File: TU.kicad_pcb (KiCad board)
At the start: 4 copper layers, 48.3 x 109.2 mm, 134 parts, among them IC1 CC1190, J1 Conn_01x06_Male, J2 Conn_01x17_Male, J3 Conn_01x05_Male, J4 Debugger connector, J5 ARM_JTAG_SWD_10, J6 Conn_01x05_Male, U1 ADP150AUJZ-3.3-R7, U2 SN65HVD233, U3 CC1200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

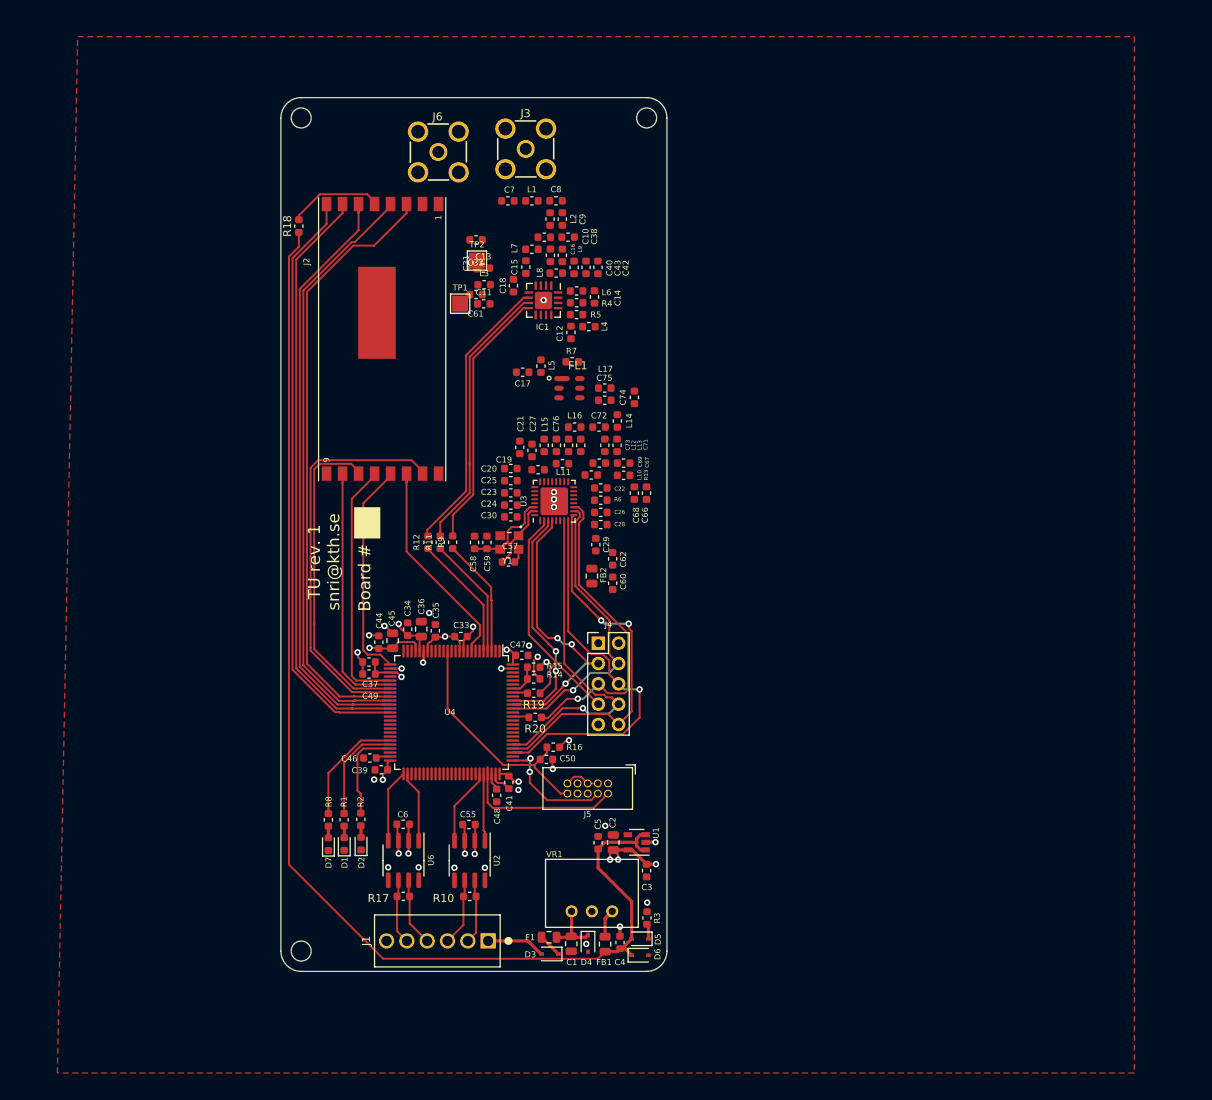
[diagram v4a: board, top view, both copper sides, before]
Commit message: Routed power for RF
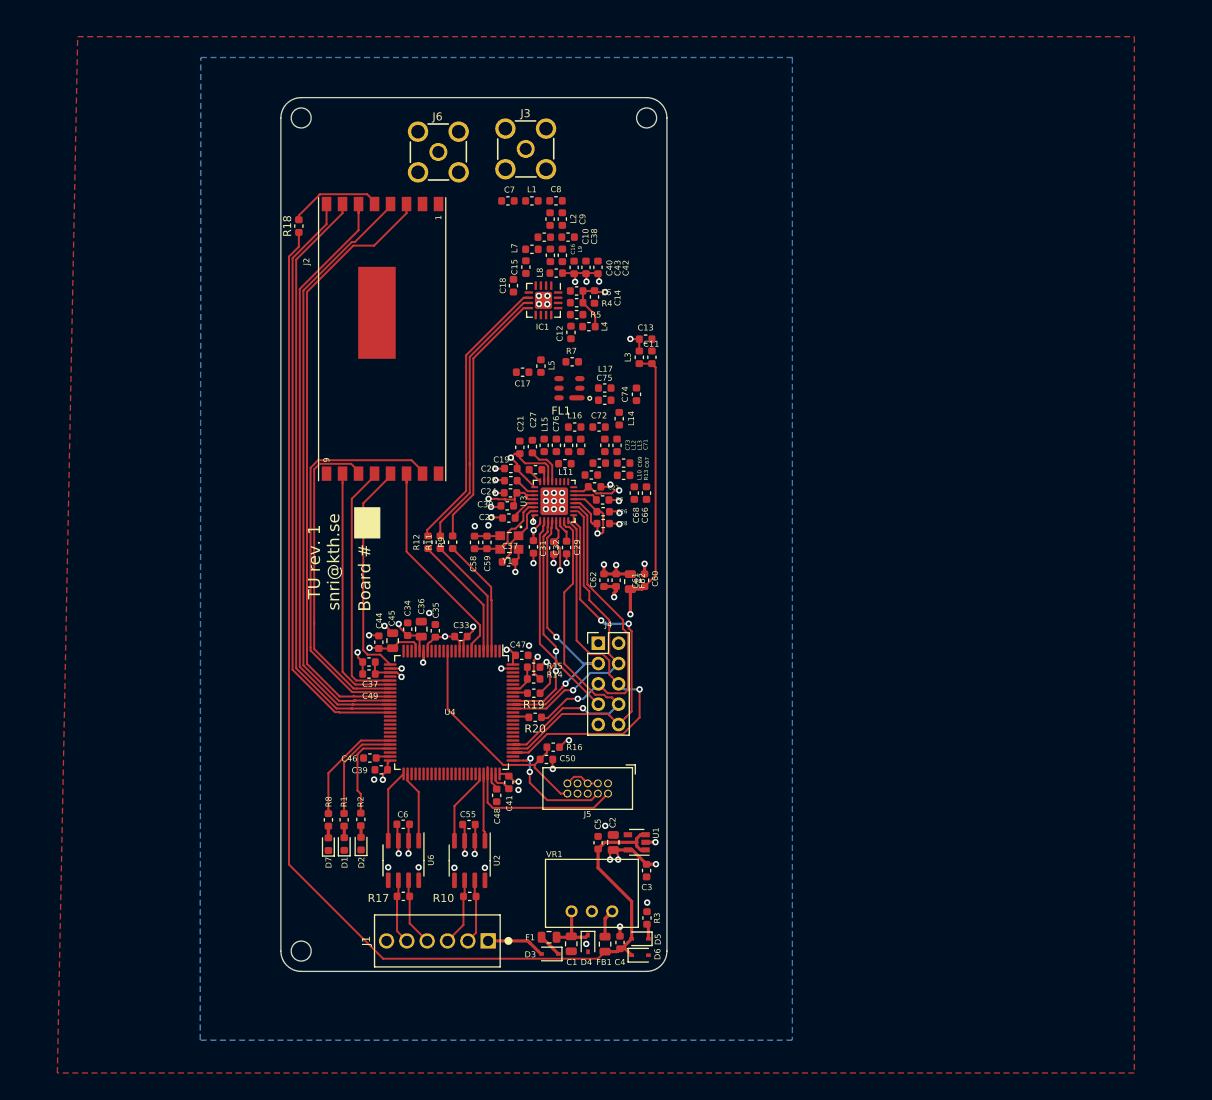
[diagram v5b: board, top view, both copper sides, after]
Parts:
- removed TP1: VDD_CC1190, TestPoint:TestPoint_Pad_2.0x2.0mm
- removed TP2: VDD_CC1200, TestPoint:TestPoint_Pad_2.0x2.0mm
- moved C61 39.8 mm to (113.0, 90.8), turned to 270 degrees
- moved C32 39.0 mm to (102.7, 86.6), turned to 270 degrees
- moved C31 36.9 mm to (105.2, 86.8)
- moved C13 22.1 mm to (116.7, 60.7)
- moved C11 22.1 mm to (117.5, 62.9), turned to 90 degrees
- moved L3 21.4 mm to (115.9, 62.9), turned to 90 degrees
- moved FB2 4.87 mm to (114.8, 91.0)
- moved C60 4.01 mm to (116.6, 90.8)
- moved C29 3.67 mm to (106.8, 86.7)
- moved C23 3.15 mm to (99.6, 83.0)
- moved C62 2.89 mm to (111.5, 90.8), turned to 270 degrees
- moved C24 1.53 mm to (99.8, 79.9)
- moved C30 1.45 mm to (99.4, 81.5)
- moved C22 0.79 mm to (110.3, 79.1)
- moved C27 0.48 mm to (102.6, 74.1)
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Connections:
- net Net-(C13-Pad1) renamed /CC1190/VDD_CC1190
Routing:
- net /transceiver/VDD_CC1200: track 0.00 -> 57.1 mm, vias 0 -> 8
- net +3V3: track 55.1 -> 90.1 mm, vias 14 -> 15
- net GND: track 36.9 -> 61.7 mm, vias 28 -> 55
- net /CC1190/VDD_CC1190: track 0.00 -> 18.3 mm, vias 0 -> 5
- net Net-(C27-Pad1): track 0.00 -> 5.19 mm
- net Net-(C23-Pad1): track 0.00 -> 4.14 mm
- net Net-(R6-Pad2): track 0.00 -> 3.06 mm
- net Net-(C29-Pad1): track 0.00 -> 2.95 mm
- net Net-(C25-Pad1): track 0.00 -> 2.74 mm
- net Net-(C19-Pad2): track 0.00 -> 1.96 mm
- net Net-(C19-Pad1): track 0.00 -> 1.51 mm
- net /transceiver/GPIO3: track 29.4 -> 28.2 mm
- net /MOSI: track 43.5 -> 44.6 mm
- net /~RESET: track 32.0 -> 30.9 mm
- net /GPIO0: track 37.6 -> 36.7 mm
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- added copper zone on In2.Cu, net /CC1190/VDD_CC1190
- added copper zone on In2.Cu, net /transceiver/VDD_CC1200
- added copper zone on B.Cu, net GND

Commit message: Feedback from peer review
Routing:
- net Net-(J2-Pad5): track 12.1 -> 13.0 mm

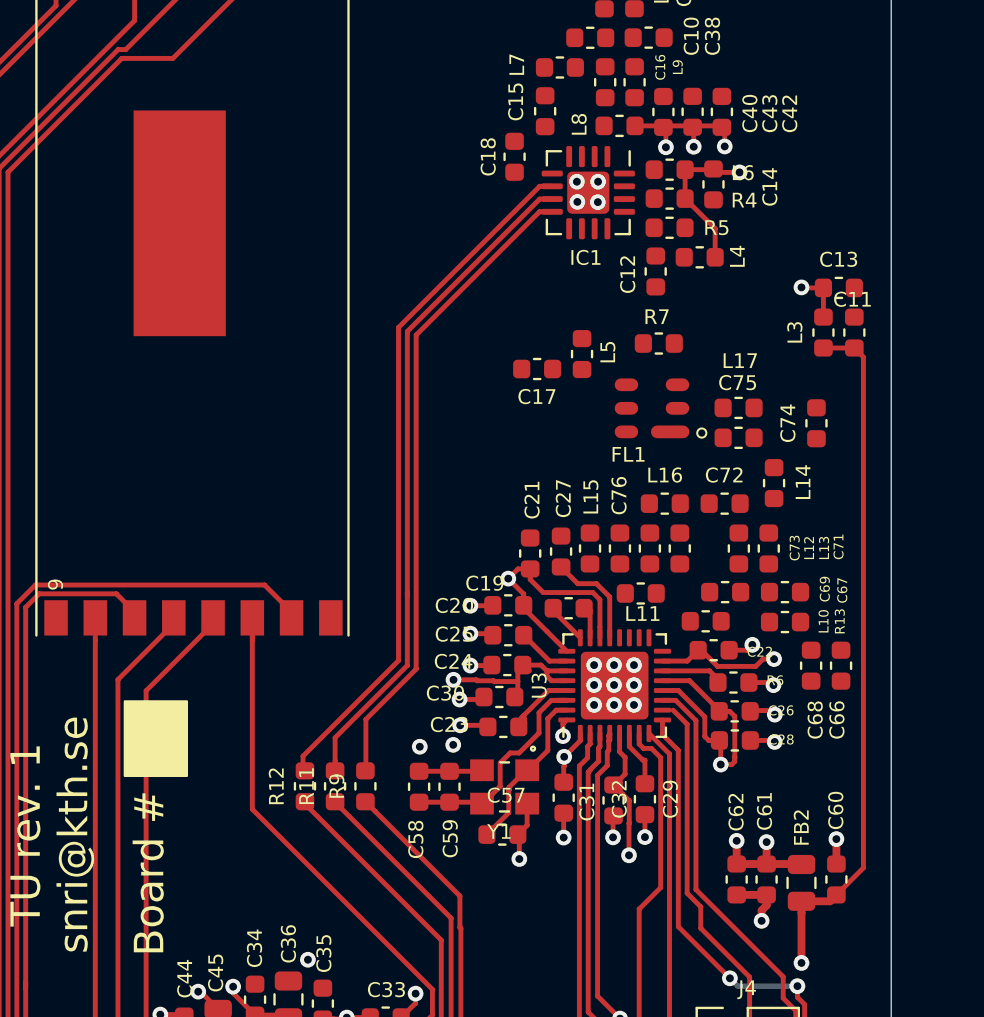
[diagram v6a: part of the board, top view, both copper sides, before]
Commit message: Added heatpad vias for extra rf module.
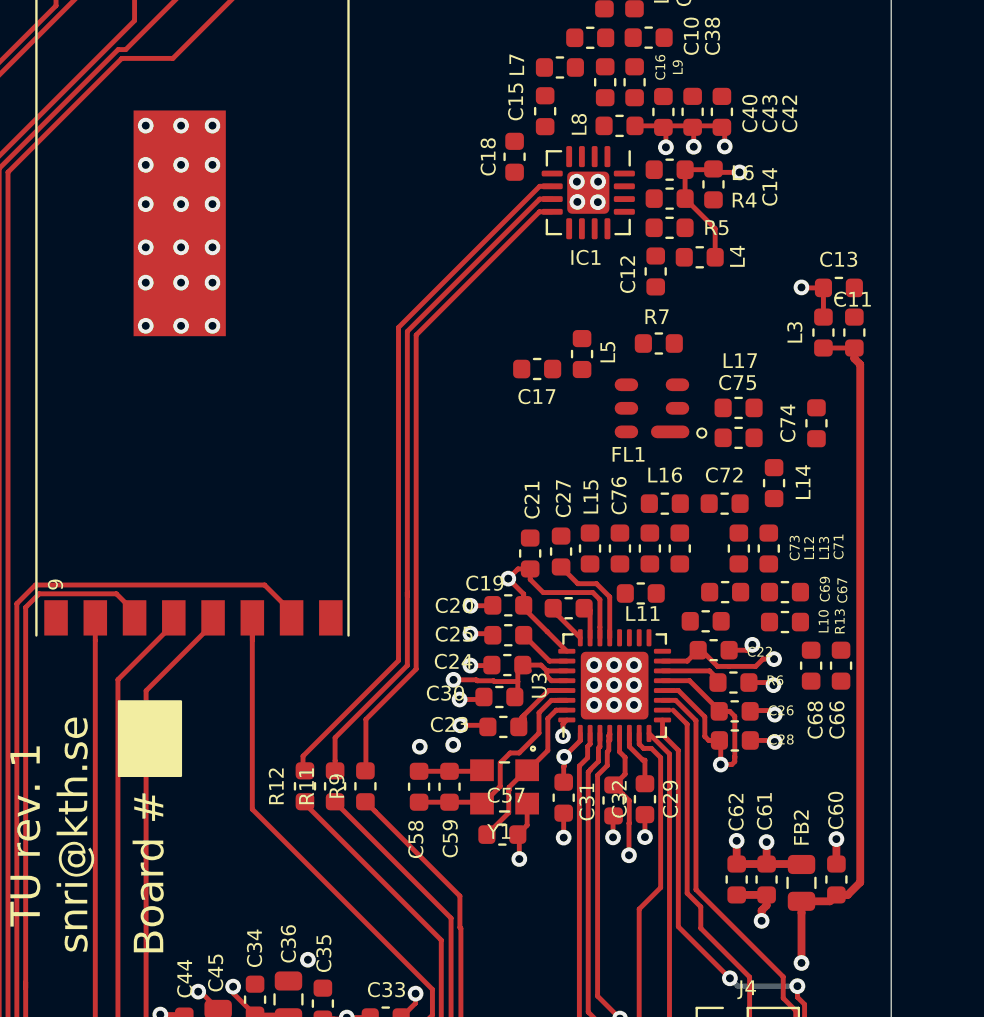
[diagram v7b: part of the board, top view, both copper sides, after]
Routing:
- net GND: vias 55 -> 73
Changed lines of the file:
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@@
     (thickness 1.6)
     (drawings 28)
-    (tracks 799)
+    (tracks 819)
     (zones 0)
     (modules 132)
@@
   )
   (setup
-    (last_trace_width 0.25)
+    (last_trace_width 0.4)
     (user_trace_width 0.4)
     (trace_clearance 0.2)
@@
     (effects (font (size 1.5 1.5) (thickness 0.3)))
   )
-  (gr_poly (pts (xy 80.3275 85.5345) (xy 83.5025 85.5345) (xy 83.5025 81.7245) (xy 80.3275 81.7245)) (layer F.SilkS) (width 0.1))
+  (gr_poly (pts (xy 80.025 85.5345) (xy 83.2 85.5345) (xy 83.2 81.7245) (xy 80.025 81.7245)) (layer F.SilkS) (width 0.1))
   (gr_text "TU rev. 1\nsnri@kth.se\n" (at 76.5175 88.519 90) (layer F.SilkS)
     (effects (font (size 1.5 1.5) (thickness 0.3)))
   )
+  (via (at 81.4 62.6) (size 0.8) (drill 0.4) (layers F.Cu B.Cu) (net 1))
+  (via (at 84.8 62.6) (size 0.8) (drill 0.4) (layers F.Cu B.Cu) (net 1))
+  (via (at 83.2 62.6) (size 0.8) (drill 0.4) (layers F.Cu B.Cu) (net 1))
+  (via (at 81.4 60.4) (size 0.8) (drill 0.4) (layers F.Cu B.Cu) (net 1))
+  (via (at 84.8 60.4) (size 0.8) (drill 0.4) (layers F.Cu B.Cu) (net 1))
+  (via (at 83.2 60.4) (size 0.8) (drill 0.4) (layers F.Cu B.Cu) (net 1))
+  (via (at 81.4 58.6) (size 0.8) (drill 0.4) (layers F.Cu B.Cu) (net 1))
+  (via (at 84.8 58.6) (size 0.8) (drill 0.4) (layers F.Cu B.Cu) (net 1))
+  (via (at 83.2 58.6) (size 0.8) (drill 0.4) (layers F.Cu B.Cu) (net 1))
+  (via (at 81.4 56.4) (size 0.8) (drill 0.4) (layers F.Cu B.Cu) (net 1))
+  (via (at 84.8 56.4) (size 0.8) (drill 0.4) (layers F.Cu B.Cu) (net 1))
+  (via (at 83.2 56.4) (size 0.8) (drill 0.4) (layers F.Cu B.Cu) (net 1))
+  (via (at 81.4 54.4) (size 0.8) (drill 0.4) (layers F.Cu B.Cu) (net 1))
+  (via (at 84.8 54.4) (size 0.8) (drill 0.4) (layers F.Cu B.Cu) (net 1))
+  (via (at 83.2 54.4) (size 0.8) (drill 0.4) (layers F.Cu B.Cu) (net 1))
+  (via (at 84.8 52.4) (size 0.8) (drill 0.4) (layers F.Cu B.Cu) (net 1))
+  (via (at 83.2 52.4) (size 0.8) (drill 0.4) (layers F.Cu B.Cu) (net 1))
+  (via (at 81.4 52.4) (size 0.8) (drill 0.4) (layers F.Cu B.Cu) (net 1))
   (via (at 104.4321 56.2991) (size 0.8) (drill 0.4) (layers F.Cu B.Cu) (net 1))
   (via (at 103.3907 56.2864) (size 0.8) (drill 0.4) (layers F.Cu B.Cu) (net 1))
@@
   (segment (start 114.808 94.742) (end 114.808 94.742) (width 0.4) (layer F.Cu) (net 3))
   (via (at 114.808 95.0595) (size 0.8) (drill 0.4) (layers F.Cu B.Cu) (net 3))
-  (segment (start 117.962012 64.190312) (end 117.5004 63.7287) (width 0.25) (layer F.Cu) (net 3))
-  (segment (start 117.962012 90.216488) (end 117.962012 64.190312) (width 0.25) (layer F.Cu) (net 3))
-  (segment (start 116.586 91.5925) (end 117.962012 90.216488) (width 0.25) (layer F.Cu) (net 3))
+  (segment (start 117.161 91.5925) (end 117.8 90.9535) (width 0.4) (layer F.Cu) (net 3))
+  (segment (start 116.586 91.5925) (end 117.161 91.5925) (width 0.4) (layer F.Cu) (net 3))
+  (segment (start 117.5004 64.2662) (end 117.5004 63.7287) (width 0.4) (layer F.Cu) (net 3))
+  (segment (start 117.8 64.5658) (end 117.5004 64.2662) (width 0.4) (layer F.Cu) (net 3))
+  (segment (start 117.8 90.9535) (end 117.8 64.5658) (width 0.4) (layer F.Cu) (net 3))
   (segment (start 116.076838 122.61614) (end 116.70184 122.61614) (width 0.4) (layer F.Cu) (net 4))
   (segment (start 115.5993 123.093678) (end 116.076838 122.61614) (width 0.4) (layer F.Cu) (net 4))

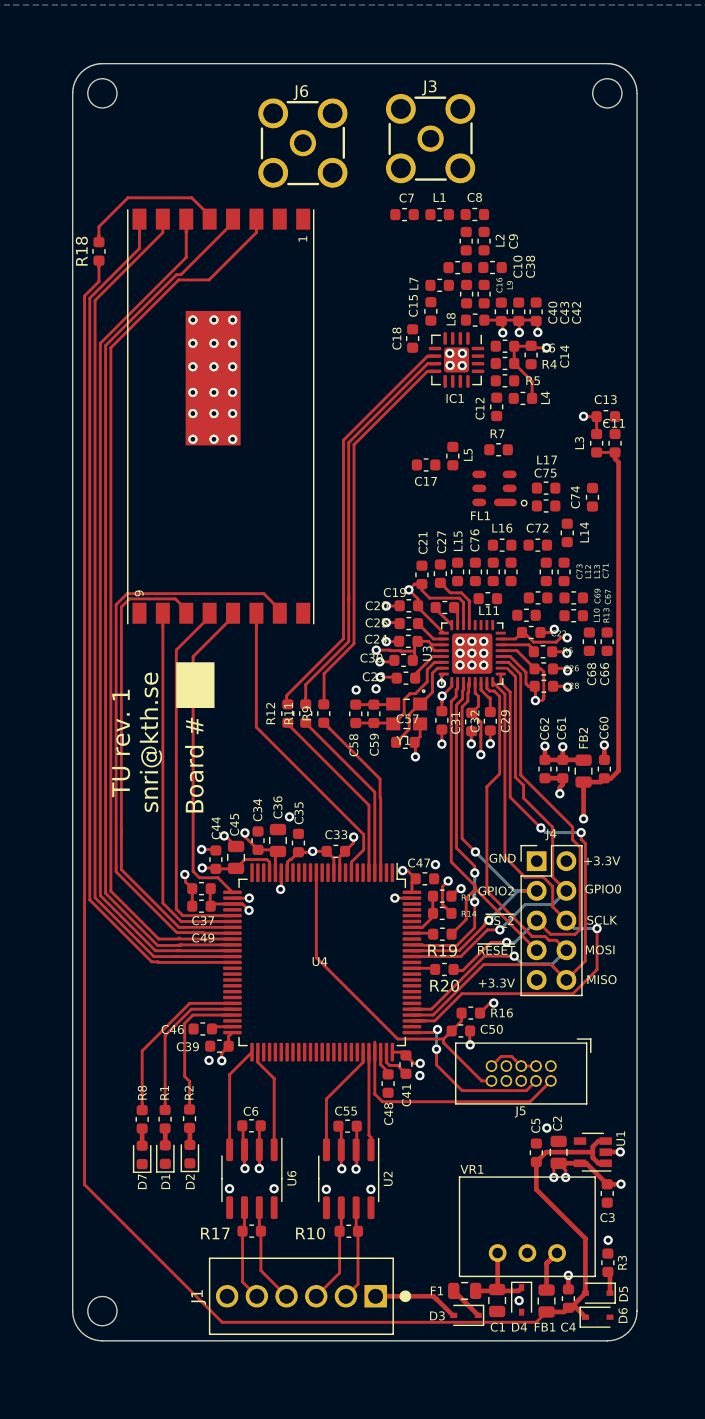
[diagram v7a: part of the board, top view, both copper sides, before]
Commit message: Made sections clearer and cleaned up silkscreen.
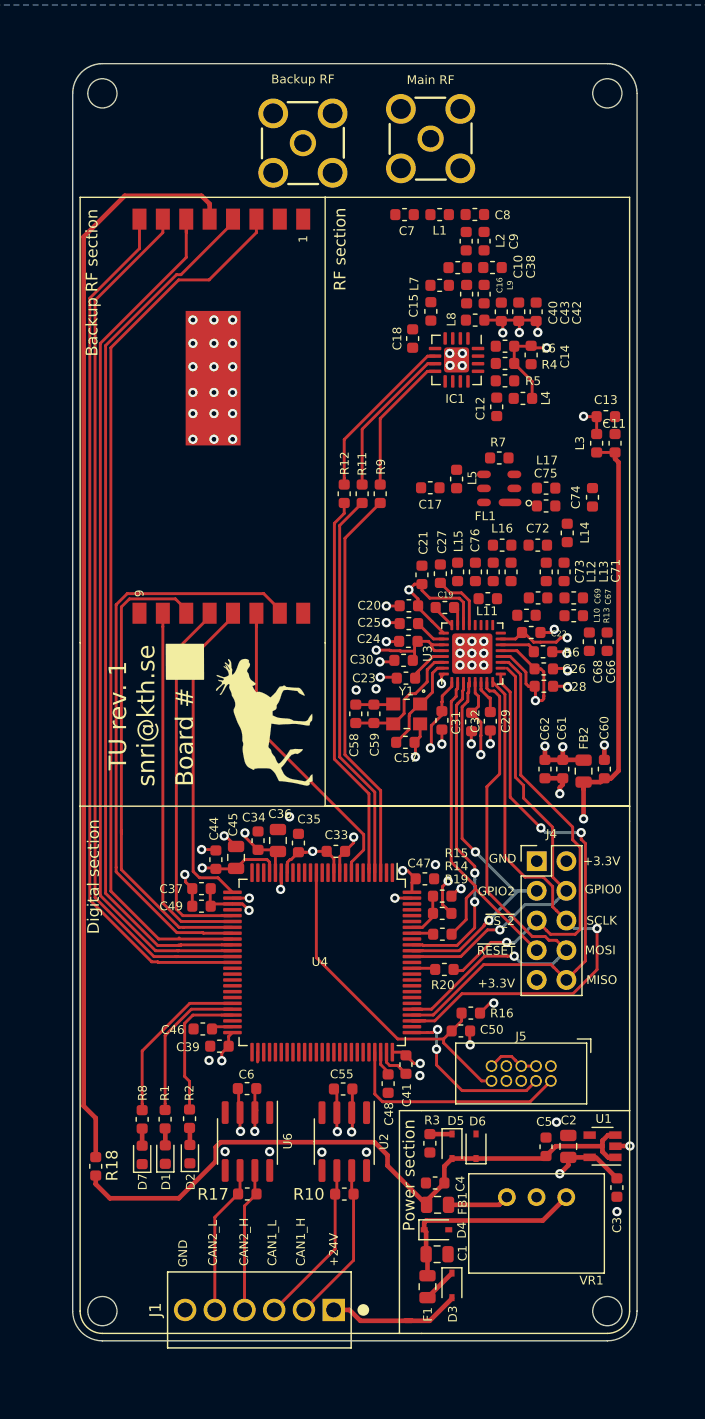
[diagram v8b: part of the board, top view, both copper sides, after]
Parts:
- added G***: LOGO, KTHFS:simon_richter, F.Cu at (87.5, 86.8)
- added H4: MountingHole, MountingHole:MountingHole_2.5mm, F.Cu at (116.8, 137.2)
- moved R18 78.2 mm to (73.1, 124.8)
- moved R11 19.4 mm to (95.9, 67.3)
- moved R12 19.4 mm to (94.3, 67.3)
- moved R9 19.4 mm to (97.4, 67.3)
- moved R3 18.3 mm to (101.7, 122.8), turned to 270 degrees
- moved D5 17.9 mm to (105.6, 123.1), turned to 90 degrees
- moved D6 17.7 mm to (103.6, 123.1), turned to 270 degrees
- moved VR1 15.2 mm to (116.6, 125.4), turned to 180 degrees
- moved C4 15.1 mm to (102.1, 126.2), turned to 180 degrees
- moved FB1 12.4 mm to (102.3, 128.1), turned to 0 degrees
- moved D4 9.43 mm to (102.2, 130.2), turned to 0 degrees
- moved C1 6.49 mm to (102.3, 132.3), turned to 0 degrees
- moved J1 3.78 mm to (87.1, 137.1)
- moved R10 3.20 mm to (94.3, 127.2)
- moved C6 3.20 mm to (86.0, 118.1)
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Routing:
- net +5V: track 152.3 -> 56.7 mm
- net Net-(J2-Pad5): track 13.0 -> 92.9 mm
- net Net-(IC1-Pad7): track 34.3 -> 13.3 mm
- net Net-(IC1-Pad6): track 35.4 -> 14.6 mm
- net Net-(IC1-Pad8): track 32.8 -> 12.0 mm
- net /CC1190/HGM: track 14.8 -> 34.1 mm
- net /CC1190/LNA_EN: track 15.2 -> 33.7 mm
- net /CC1190/PA_EN: track 15.8 -> 33.2 mm
- net +24V: track 7.11 -> 17.7 mm
- net /CAN_transceiver/CAN_RX_1: track 9.65 -> 0.00 mm
- net /CAN_transceiver/CAN_RX_2: track 9.14 -> 0.00 mm
- net /CAN_transceiver/CAN_TX_1: track 8.43 -> 0.00 mm
- net /CAN_transceiver/CAN_TX_2: track 8.94 -> 0.85 mm
- net /CAN_transceiver/CANL_1: track 8.46 -> 14.1 mm
- net /CAN_transceiver/CANH_1: track 8.06 -> 13.7 mm
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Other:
- board text added: "Backup RF"
- board text added: "Backup RF section"
- board text added: "Digital section"
- board text added: "Main RF"
- board text added: "Power section"
- board text added: "RF section"
